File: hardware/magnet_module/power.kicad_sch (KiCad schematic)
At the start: 30 parts, among them J20 Barrel_Jack, U12 TPS565208, U9 TPS561201

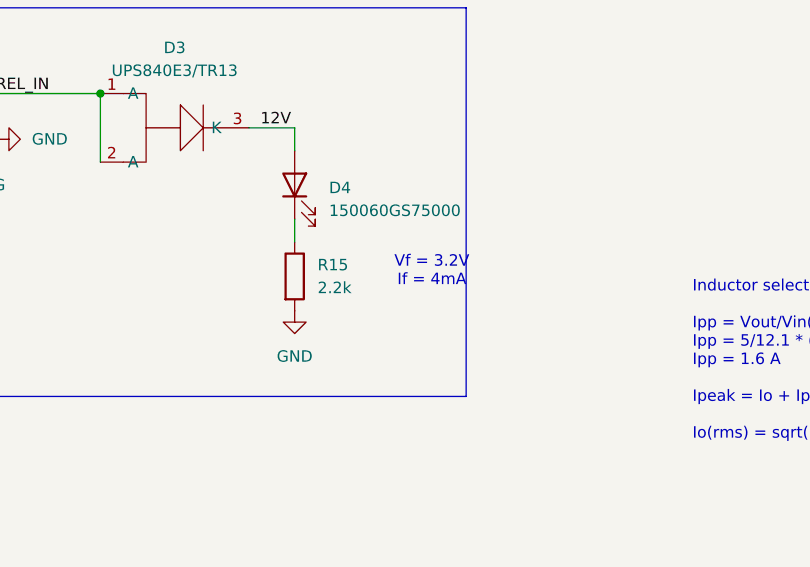
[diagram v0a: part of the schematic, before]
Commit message: reduce LED brightness
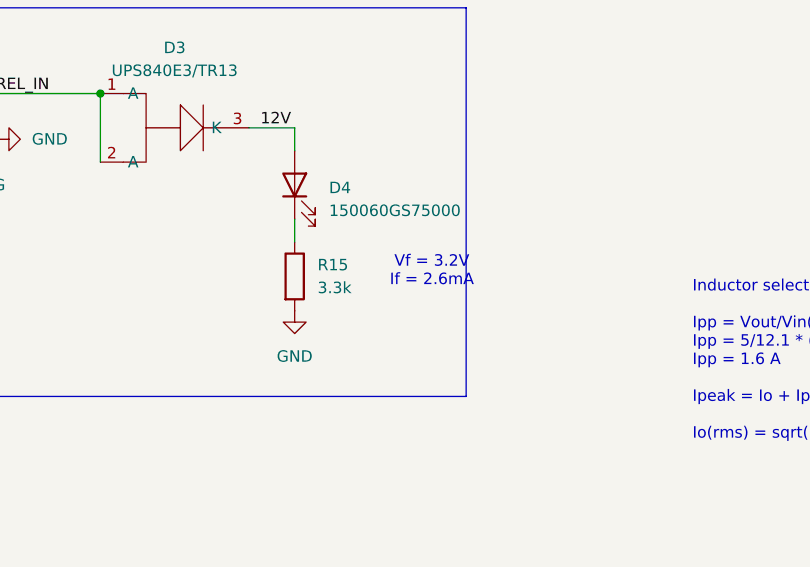
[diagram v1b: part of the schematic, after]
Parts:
- R15: value 2.2k -> 3.3k; LCSC C4190 -> C22978; MPN 0603WAF2201T5E -> 0603WAF3301T5E
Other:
- note added: "Vf = 3.2V If = 2.6mA"
- note removed: "Vf = 3.2V If = 4mA"
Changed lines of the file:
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@@
 		)
 	)
-	(text "Vf = 3.2V\nIf = 4mA"
+	(text "Vf = 3.2V\nIf = 2.6mA"
 		(exclude_from_sim no)
 		(at 91.44 47.752 0)
@@
 			)
 		)
-		(property "Value" "2.2k"
+		(property "Value" "3.3k"
 			(at 78.74 49.5299 0)
 			(effects
@@
 			)
 		)
-		(property "MPN" "0603WAF2201T5E"
+		(property "MPN" "0603WAF3301T5E"
 			(at 76.2 48.26 0)
 			(effects
@@
 			)
 		)
-		(property "LCSC" "C4190"
+		(property "LCSC" "C22978"
 			(at 76.2 48.26 0)
 			(effects
